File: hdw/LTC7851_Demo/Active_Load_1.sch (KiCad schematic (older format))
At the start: 0 parts

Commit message: Added active load sheets
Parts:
- added J? (x2): ISNS, symbol Connector_Generic:Conn_01x02
- added J?: FG_LOAD, symbol Connector_Generic:Conn_01x02
- added Q? (x2): BSC123N10LSGATMA1, Package_TO_SOT_SMD:TDSON-8-1, symbol Transistor_FET:BSC123N10LSG
- added R? (x2): 5m, symbol Custom_Library:R_Custom
- added R? (x4): 10k, symbol Custom_Library:R_Custom
- added R? (x2): 10, symbol Custom_Library:R_Custom
- added U?: LT1010DD, Housings_DFN_QFN:DFN-8-1EP_3x3mm_Pitch0.5mm, symbol Custom_Library:LT1010DD
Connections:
- net labels added: +12V, +5V, GND, LOAD_GATE
- wire segments 0 -> 18

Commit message: Filled in power input page
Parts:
- added C?: 1uF, symbol Custom_Library:C_Custom
- added C?: 0.1uF, symbol Custom_Library:C_Custom
- added C?: 10uF, symbol Custom_Library:CP_Tant_Custom
- R?: value 10k -> 10

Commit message: Annotated schematic
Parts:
- gave numbers to parts that had none: 17

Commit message: Added Digi-Key part numbers for all parts
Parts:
- C1101: Digi-Key PN PN -> 1276-6524-1-ND
- C1102: Digi-Key PN PN -> 490-4779-1-ND
- R1101, R1105, R1106: Digi-Key PN PN -> RHM10KADCT-ND
- R1102, R1103, R1104: Digi-Key PN PN -> YAG3351CT-ND
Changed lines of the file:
@@
 F 5 "1%" H 7320 2640 50  0000 L CNN "Tolerance"
 F 6 "1/10W" H 7320 2560 50  0000 L CNN "Wattage"
-F 7 "PN" H 7540 3040 60  0001 C CNN "Digi-Key PN"
+F 7 "RHM10KADCT-ND" H 7540 3040 60  0001 C CNN "Digi-Key PN"
 	1    7240 2640
 	1    0    0    -1
@@
 F 5 "1%" V 6760 2420 50  0000 C CNN "Tolerance"
 F 6 "1/10W" V 6860 2420 50  0000 C CNN "Wattage"
-F 7 "PN" H 6860 2820 60  0001 C CNN "Digi-Key PN"
+F 7 "YAG3351CT-ND" H 6860 2820 60  0001 C CNN "Digi-Key PN"
 	1    6560 2420
 	0    1    1    0
@@
 F 5 "1%" H 3340 2980 50  0000 L CNN "Tolerance"
 F 6 "1/10W" H 3340 2900 50  0000 L CNN "Wattage"
-F 7 "PN" H 3560 3380 60  0001 C CNN "Digi-Key PN"
+F 7 "YAG3351CT-ND" H 3560 3380 60  0001 C CNN "Digi-Key PN"
 	1    3260 2980
 	1    0    0    -1
@@
 F 5 "1%" H 2580 3730 50  0000 L CNN "Tolerance"
 F 6 "1/10W" H 2580 3650 50  0000 L CNN "Wattage"
-F 7 "PN" H 2800 4130 60  0001 C CNN "Digi-Key PN"
+F 7 "RHM10KADCT-ND" H 2800 4130 60  0001 C CNN "Digi-Key PN"
 	1    2500 3730
 	-1   0    0    -1
@@
 F 5 "1%" H 7320 4680 50  0000 L CNN "Tolerance"
 F 6 "1/10W" H 7320 4600 50  0000 L CNN "Wattage"
-F 7 "PN" H 7540 5080 60  0001 C CNN "Digi-Key PN"
+F 7 "RHM10KADCT-ND" H 7540 5080 60  0001 C CNN "Digi-Key PN"
 	1    7240 4680
 	1    0    0    -1
@@
 F 5 "1%" V 6760 4460 50  0000 C CNN "Tolerance"
 F 6 "1/10W" V 6860 4460 50  0000 C CNN "Wattage"
-F 7 "PN" H 6860 4860 60  0001 C CNN "Digi-Key PN"
+F 7 "YAG3351CT-ND" H 6860 4860 60  0001 C CNN "Digi-Key PN"
 	1    6560 4460
 	0    1    1    0
@@
 F 5 "16V" H 2490 4780 50  0000 R CNN "Voltage"
 F 6 "X7R" H 2490 4680 50  0000 R CNN "Dielectric"
-F 7 "PN" H 3065 5280 60  0001 C CNN "Digi-Key PN"
+F 7 "1276-6524-1-ND" H 3065 5280 60  0001 C CNN "Digi-Key PN"
 	1    2640 4780
 	1    0    0    -1
@@
 F 5 "50V" H 3160 4780 50  0000 R CNN "Voltage"
 F 6 "X7R" H 3160 4680 50  0000 R CNN "Dielectric"
-F 7 "PN" H 3735 5280 60  0001 C CNN "Digi-Key PN"
+F 7 "490-4779-1-ND" H 3735 5280 60  0001 C CNN "Digi-Key PN"
 	1    3310 4780
 	1    0    0    -1

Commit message: Assigned footprints
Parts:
- C1101, C1102: footprint (none) -> Capacitors_SMD:C_0603
- C1103: footprint (none) -> Capacitors_Tantalum_SMD:CP_Tantalum_Case-B_EIA-3528-21_Reflow
- J1101, J1102, J1103: footprint (none) -> Pin_Headers:Pin_Header_Straight_1x02_Pitch2.54mm
- Q1101, Q1102: footprint Package_TO_SOT_SMD:TDSON-8-1 -> TO_SOT_Packages_SMD:TDSON-8-1
- R1101, R1102, R1103, R1104, R1105, R1106: footprint (none) -> Resistors_SMD:R_0603
- R1107, R1108: footprint (none) -> Resistors_SMD:R_2512
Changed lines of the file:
@@
 F 0 "Q1101" H 8100 2495 50  0000 L CNN
 F 1 "BSC123N10LSGATMA1" H 8100 2420 50  0000 L CNN
-F 2 "Package_TO_SOT_SMD:TDSON-8-1" H 8100 2345 50  0001 L CIN
+F 2 "TO_SOT_Packages_SMD:TDSON-8-1" H 8100 2345 50  0001 L CIN
 F 3 "http://www.infineon.com/dgdl/Infineon-BSC123N10LS-DS-v02_08-en.pdf?fileId=db3a30431b3e89eb011b4626974b7df5" V 7900 2420 50  0001 L CNN
 F 4 "BSC123N10LSGATMA1CT-ND" H 7900 2420 50  0001 C CNN "Digi-Key PN"
@@
 F 0 "J1102" H 8830 2800 50  0000 C CNN
 F 1 "ISNS" H 8830 2500 50  0000 C CNN
-F 2 "" H 8830 2700 50  0001 C CNN
+F 2 "Pin_Headers:Pin_Header_Straight_1x02_Pitch2.54mm" H 8830 2700 50  0001 C CNN
 F 3 "~" H 8830 2700 50  0001 C CNN
 	1    8830 2700
@@
 F 0 "R1107" H 7900 2940 50  0000 R CNN
 F 1 "5m" V 8000 2940 50  0000 C CNN
-F 2 "" H 8000 2940 50  0001 C CNN
+F 2 "Resistors_SMD:R_2512" H 8000 2940 50  0001 C CNN
 F 3 "" H 8000 2940 50  0001 C CNN
 F 4 "YAG2145CT-ND" H 8300 3340 60  0001 C CNN "Digi-Key PN"
@@
 F 0 "R1105" H 7140 2640 50  0000 R CNN
 F 1 "10k" V 7240 2640 50  0000 C CNN
-F 2 "" H 7240 2640 50  0001 C CNN
+F 2 "Resistors_SMD:R_0603" H 7240 2640 50  0001 C CNN
 F 3 "" H 7240 2640 50  0001 C CNN
 F 4 "0603" H 7320 2720 50  0000 L CNN "display_footprint"
@@
 F 0 "R1103" V 6460 2420 50  0000 C CNN
 F 1 "10" V 6560 2420 50  0000 C CNN
-F 2 "" H 6560 2420 50  0001 C CNN
+F 2 "Resistors_SMD:R_0603" H 6560 2420 50  0001 C CNN
 F 3 "" H 6560 2420 50  0001 C CNN
 F 4 "0603" V 6660 2420 50  0000 C CNN "display_footprint"
@@
 F 0 "R1102" H 3340 3130 50  0000 L CNN
 F 1 "10" V 3260 2980 50  0000 C CNN
-F 2 "" H 3260 2980 50  0001 C CNN
+F 2 "Resistors_SMD:R_0603" H 3260 2980 50  0001 C CNN
 F 3 "" H 3260 2980 50  0001 C CNN
 F 4 "0603" H 3340 3060 50  0000 L CNN "display_footprint"
@@
 F 0 "J1101" H 1670 3610 50  0000 C CNN
 F 1 "FG_LOAD" H 1670 3310 50  0000 C CNN
-F 2 "" H 1670 3510 50  0001 C CNN
+F 2 "Pin_Headers:Pin_Header_Straight_1x02_Pitch2.54mm" H 1670 3510 50  0001 C CNN
 F 3 "~" H 1670 3510 50  0001 C CNN
 	1    1670 3510
@@
 F 0 "R1101" H 2400 3730 50  0000 R CNN
 F 1 "10k" V 2500 3730 50  0000 C CNN
-F 2 "" H 2500 3730 50  0001 C CNN
+F 2 "Resistors_SMD:R_0603" H 2500 3730 50  0001 C CNN
 F 3 "" H 2500 3730 50  0001 C CNN
 F 4 "0603" H 2580 3810 50  0000 L CNN "display_footprint"
@@
 F 0 "Q1102" H 8100 4535 50  0000 L CNN
 F 1 "BSC123N10LSGATMA1" H 8100 4460 50  0000 L CNN
-F 2 "Package_TO_SOT_SMD:TDSON-8-1" H 8100 4385 50  0001 L CIN
+F 2 "TO_SOT_Packages_SMD:TDSON-8-1" H 8100 4385 50  0001 L CIN
 F 3 "http://www.infineon.com/dgdl/Infineon-BSC123N10LS-DS-v02_08-en.pdf?fileId=db3a30431b3e89eb011b4626974b7df5" V 7900 4460 50  0001 L CNN
 F 4 "BSC123N10LSGATMA1CT-ND" H 7900 4460 50  0001 C CNN "Digi-Key PN"
@@
 F 0 "J1103" H 8830 4840 50  0000 C CNN
 F 1 "ISNS" H 8830 4540 50  0000 C CNN
-F 2 "" H 8830 4740 50  0001 C CNN
+F 2 "Pin_Headers:Pin_Header_Straight_1x02_Pitch2.54mm" H 8830 4740 50  0001 C CNN
 F 3 "~" H 8830 4740 50  0001 C CNN
 	1    8830 4740
@@
 F 0 "R1108" H 7900 4980 50  0000 R CNN
 F 1 "5m" V 8000 4980 50  0000 C CNN
-F 2 "" H 8000 4980 50  0001 C CNN
+F 2 "Resistors_SMD:R_2512" H 8000 4980 50  0001 C CNN
 F 3 "" H 8000 4980 50  0001 C CNN
 F 4 "YAG2145CT-ND" H 8300 5380 60  0001 C CNN "Digi-Key PN"
@@
 F 0 "R1106" H 7140 4680 50  0000 R CNN
 F 1 "10k" V 7240 4680 50  0000 C CNN
-F 2 "" H 7240 4680 50  0001 C CNN
+F 2 "Resistors_SMD:R_0603" H 7240 4680 50  0001 C CNN
 F 3 "" H 7240 4680 50  0001 C CNN
 F 4 "0603" H 7320 4760 50  0000 L CNN "display_footprint"
@@
 F 0 "R1104" V 6460 4460 50  0000 C CNN
 F 1 "10" V 6560 4460 50  0000 C CNN
-F 2 "" H 6560 4460 50  0001 C CNN
+F 2 "Resistors_SMD:R_0603" H 6560 4460 50  0001 C CNN
 F 3 "" H 6560 4460 50  0001 C CNN
 F 4 "0603" V 6660 4460 50  0000 C CNN "display_footprint"
@@
 F 0 "C1101" H 2665 4880 50  0000 L CNN
 F 1 "1uF" H 2665 4680 50  0000 L CNN
-F 2 "" H 2678 4630 50  0001 C CNN
+F 2 "Capacitors_SMD:C_0603" H 2678 4630 50  0001 C CNN
 F 3 "" H 2665 4880 50  0001 C CNN
 F 4 "0603" H 2490 4880 50  0000 R CNN "display_footprint"
@@
 F 0 "C1102" H 3335 4880 50  0000 L CNN
 F 1 "0.1uF" H 3335 4680 50  0000 L CNN
-F 2 "" H 3348 4630 50  0001 C CNN
+F 2 "Capacitors_SMD:C_0603" H 3348 4630 50  0001 C CNN
 F 3 "" H 3335 4880 50  0001 C CNN
 F 4 "0603" H 3160 4880 50  0000 R CNN "display_footprint"
@@
 F 0 "C1103" H 3945 4880 50  0000 L CNN
 F 1 "10uF" H 3945 4680 50  0000 L CNN
-F 2 "" H 3958 4630 50  0001 C CNN
+F 2 "Capacitors_Tantalum_SMD:CP_Tantalum_Case-B_EIA-3528-21_Reflow" H 3958 4630 50  0001 C CNN
 F 3 "" H 3945 4880 50  0001 C CNN
 F 4 "399-5034-1-ND" H 3920 4780 50  0001 C CNN "Digi-Key PN"

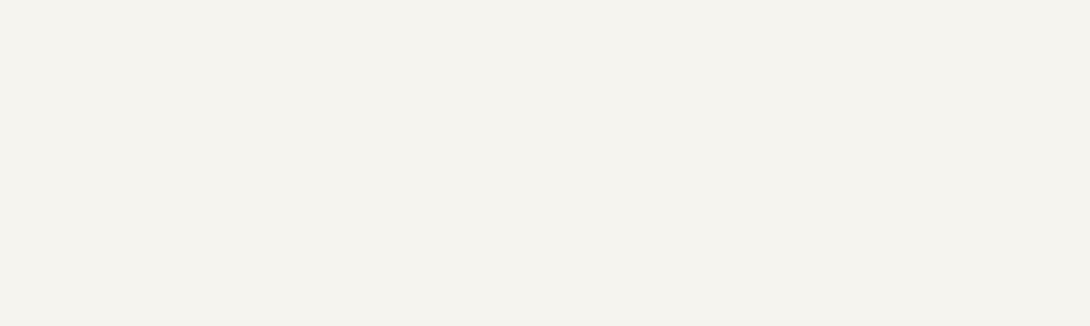
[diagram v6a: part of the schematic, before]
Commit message: Added page titles
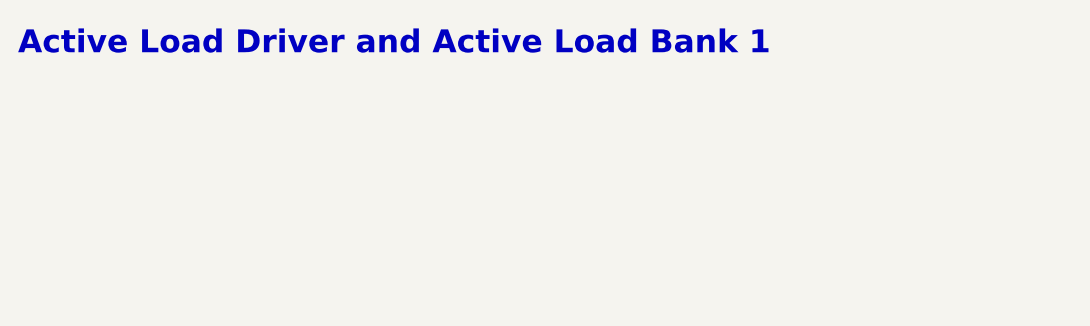
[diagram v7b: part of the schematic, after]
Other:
- note added: "Active Load Driver and Active Load Bank 1"
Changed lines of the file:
@@
 	1    0    0    -1
 $EndComp
+Text Notes 540  690  0    100  ~ 20
+Active Load Driver and Active Load Bank 1
 $EndSCHEMATC

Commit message: Placed phases on board
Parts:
- removed J1103: ISNS, Pin_Headers:Pin_Header_Straight_1x02_Pitch2.54mm, symbol Connector_Generic:Conn_01x02
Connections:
- wire segments 18 -> 16
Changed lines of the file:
@@
 	1    0    0    -1
 $EndComp
-Wire Wire Line
-	8000 4830 8000 4740
 $Comp
 L power:GND #PWR01117
@@
 F 3 "" H 8000 5130 50  0001 C CNN
 	1    8000 5130
-	1    0    0    -1
-$EndComp
-$Comp
-L Connector_Generic:Conn_01x02 J1103
-U 1 1 5BC42834
-P 8830 4740
-F 0 "J1103" H 8830 4840 50  0000 C CNN
-F 1 "ISNS" H 8830 4540 50  0000 C CNN
-F 2 "Pin_Headers:Pin_Header_Straight_1x02_Pitch2.54mm" H 8830 4740 50  0001 C CNN
-F 3 "~" H 8830 4740 50  0001 C CNN
-	1    8830 4740
-	1    0    0    -1
-$EndComp
-Wire Wire Line
-	8630 4740 8000 4740
-Connection ~ 8000 4740
-Wire Wire Line
-	8000 4740 8000 4660
-$Comp
-L power:GND #PWR01119
-U 1 1 5BC4283E
-P 8630 4840
-F 0 "#PWR01119" H 8630 4590 50  0001 C CNN
-F 1 "GND" H 8630 4690 50  0000 C CNN
-F 2 "" H 8630 4840 50  0001 C CNN
-F 3 "" H 8630 4840 50  0001 C CNN
-	1    8630 4840
 	1    0    0    -1
 $EndComp
@@
 Text Notes 540  690  0    100  ~ 20
 Active Load Driver and Active Load Bank 1
+Wire Wire Line
+	8000 4660 8000 4830
 $EndSCHEMATC
